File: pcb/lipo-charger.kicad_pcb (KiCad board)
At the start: 2 copper layers, 48 x 48 mm, 37 parts, among them J101 Barrel_Jack, J102 Conn_01x04, J103 Conn_01x03, J104 Conn_01x03, J201 Conn_01x02, J202 Conn_01x02, P101 Polarity, P102 Outline, P103 OSHW, Q201 Q_NMOS_GSD, U101 LM317L_TO92, U201 MP2359, U202 LM358, U203 MAX4377, U204 LM358

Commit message: Massive rework, fully routed
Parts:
- removed C101: 1u, Capacitors_SMD_Round:C_0805
- removed C203: 22u, Capacitors_SMD_Round:C_1206
- removed C204: 0.1u, Capacitors_SMD_Round:C_0603
- removed D202: B230A, Diodes_SMD:D_SMA
- removed D203: B5819, Diodes_SMD:D_SOD-323_HandSoldering
- removed D204: LED, LEDs:LED_0805_HandSoldering
- removed L201: 4.7uH, Inductors_SMD:L_Taiyo-Yuden_NR-50xx
- removed Q201: Q_NMOS_GSD, TO_Combo_Packages:TO_220_247
- removed R102: 330R, Resistors_SMD:R_0603_HandSoldering
- removed R103: 2k, Resistors_SMD:R_0603_HandSoldering
- removed R104, R105: 10k, Resistors_SMD:R_0603_HandSoldering
- removed R202: 100k, Resistors_SMD:R_0603_HandSoldering
- removed R203: 0R025, Sense_Resistors:R_2512_AD_Optimized
- removed R204: 107k, Resistors_SMD:R_0603_HandSoldering
- removed R205: 25.5k, Resistors_SMD:R_0603_HandSoldering
- removed TP101, TP201: TEST, Measurement_Points:Measurement_Point_Round-SMD-Pad_Small
- removed U101: LM317L_TO92, TO_SOT_Packages_THT:TO-92_Inline_Narrow_Oval
- removed U203: MAX4377, Housings_SOIC:SOIC-8_3.9x4.9mm_Pitch1.27mm
- removed U204: LM358, Housings_SOIC:SOIC-8_3.9x4.9mm_Pitch1.27mm
- added C301: 0.1u, Capacitors_SMD_Round:C_0603, F.Cu at (159.5, 109.5)
- added C401: 10u, Capacitors_SMD_Round:C_1206, F.Cu at (138.5, 104.5)
- added C402: 10n, Capacitors_SMD_Round:C_0603, F.Cu at (146.5, 103.0)
- added C403: 22u, Capacitors_SMD_Round:C_1206, F.Cu at (148.5, 101.0)
- added D301: D_Schottky, Diodes_SMD:D_SOD-123, F.Cu at (156.0, 102.0)
- added D401: B230A, Diodes_SMD:D_SMA, F.Cu at (147.5, 111.5)
- added L401: 4.7uH, Inductors_SMD:L_Taiyo-Yuden_NR-50xx, F.Cu at (148.0, 107.0)
- added P104: Fid, Fiducials:Fiducial_1mm_Dia_2.54mm_Outer_CopperTop, F.Cu at (130.0, 120.0)
- added Q301: Q_NMOS_GDS, TO_SOT_Packages_SMD:TO-252-2, F.Cu at (146.5, 84.5)
- added Q302: Q_NMOS_GSD, TO_SOT_Packages_SMD:SOT-23_Handsoldering, F.Cu at (152.0, 92.0)
- added Q501: Q_PMOS_GSD, TO_SOT_Packages_SMD:SOT-23_Handsoldering, F.Cu at (158.5, 83.0)
- added Q502: Q_NMOS_GSD, TO_SOT_Packages_SMD:SOT-23_Handsoldering, F.Cu at (139.5, 98.5)
- added Q503: Q_PMOS_GSD, TO_SOT_Packages_SMD:SOT-23_Handsoldering, F.Cu at (158.5, 88.0)
- added R301: 100R, Resistors_SMD:R_0603_HandSoldering, F.Cu at (166.5, 104.0)
- added R302: 100k, Resistors_SMD:R_0603_HandSoldering, F.Cu at (142.0, 89.0)
- added R303: 100k, Resistors_SMD:R_0603_HandSoldering, F.Cu at (157.5, 98.5)
- added R304: 100k, Resistors_SMD:R_0603_HandSoldering, F.Cu at (154.0, 102.5)
- added R305: 100k, Resistors_SMD:R_0603_HandSoldering, F.Cu at (156.0, 112.5)
- added R401: 107k, Resistors_SMD:R_0603_HandSoldering, F.Cu at (152.0, 102.5)
- added R402: 25.5k, Resistors_SMD:R_0603_HandSoldering, F.Cu at (152.0, 107.5)
- added R501: 100k, Resistors_SMD:R_0603_HandSoldering, F.Cu at (135.5, 98.5)
- added R502: 100k, Resistors_SMD:R_0603_HandSoldering, F.Cu at (162.5, 88.0)
- added U301: LM358, Housings_SOIC:SOIC-8_3.9x4.9mm_Pitch1.27mm, F.Cu at (161.5, 106.0)
- added U401: MP2359, TO_SOT_Packages_SMD:SOT-23-6_Handsoldering, F.Cu at (143.0, 104.5)
- C201: value 10u -> 0.1u; footprint Capacitors_SMD_Round:C_1206 -> Capacitors_SMD_Round:C_0603
- C202: value 10n -> 0.1u
- J101: value Barrel_Jack -> Conn_01x04; footprint Connectors:Barrel_Jack_CUI_PJ-102AH -> Connectors_Molex:Molex_KK-6410-04_04x2.54mm_Straight
- J102: footprint Pin_Headers:Pin_Header_Straight_1x04_Pitch2.54mm -> Connectors_Molex:Molex_KK-6410-04_04x2.54mm_Straight
- J103: value Conn_01x03 -> Conn_01x04; footprint Pin_Headers:Pin_Header_Straight_1x03_Pitch2.54mm -> Connectors_Molex:Molex_KK-6410-04_04x2.54mm_Straight
- J104: footprint Pin_Headers:Pin_Header_Straight_1x03_Pitch2.54mm -> Connectors_Molex:Molex_KK-6410-03_03x2.54mm_Straight
- P101: value Polarity -> Fid; footprint Polarity_Symbols:Polarity_Center_Positive_3mm_SilkScreen -> Fiducials:Fiducial_1mm_Dia_2.54mm_Outer_CopperTop
- R101: value 0R -> 100R
- R201: value 10k -> 0R025; footprint Resistors_SMD:R_0603_HandSoldering -> Sense_Resistors:R_2512_AD_Optimized
- U201: value MP2359 -> LM358; footprint TO_SOT_Packages_SMD:SOT-23-6_Handsoldering -> Housings_SOIC:SOIC-8_3.9x4.9mm_Pitch1.27mm
- U202: value LM358 -> MAX4377
- moved P101 46.8 mm to (163.0, 80.0)
- moved U202 45.3 mm to (164.0, 97.5), turned to 180 degrees
- moved J103 44.5 mm to (172.0, 102.5), turned to 270 degrees
- moved R201 37.9 mm to (160.0, 92.5), turned to 180 degrees
- moved J104 36.6 mm to (172.0, 114.0), turned to 270 degrees
- moved R101 31.9 mm to (149.5, 117.0), turned to 180 degrees
- moved C201 28.0 mm to (162.0, 101.0), turned to 0 degrees
- moved U201 22.0 mm to (161.5, 113.0), turned to 0 degrees
- moved P103 21.9 mm to (139.5, 114.0)
- moved C202 20.5 mm to (159.5, 116.5), turned to 180 degrees
- moved J201 20.0 mm to (170.5, 90.0)
- moved J202 19.9 mm to (171.5, 82.5), turned to 180 degrees
- moved D201 18.8 mm to (154.0, 107.5), turned to 270 degrees
- moved P102 14.8 mm to (127.5, 78.0)
- moved J101 8.20 mm to (131.0, 103.0), turned to 90 degrees
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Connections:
- C201 pad 1: /charger/VIN -> +9VA
- C201 pad 2: GND -> GNDA
- C202 pad 1: Net-(C202-Pad1) -> +9VA
- C202 pad 2: /charger/Vsw -> GNDA
- D201 pad 1: Net-(D201-Pad1) -> /charger/buck/FB
- J101 pad 1: /charger/VIN -> /charger/CHG_EN
- J101 pad 2: GND -> /charger/CHG_AREF
- J101 pad 3: GND -> /charger/MASTER_EN
- J102 pad 1: /charger/CHG_AREF -> +9VA
- J102 pad 2: /charger/LOAD_VREF -> GNDA
- J102 pad 3: /charger/LOAD_AREF -> /charger/VIN
- J102 pad 4: GNDA -> /charger/GNDIN
- J103 pad 1: /charger/CHG_EN -> /charger/LOAD_EN
- J103 pad 2: /charger/LOAD_EN -> /charger/LOAD_VREF
- J103 pad 3: GNDA -> /charger/LOAD_AREF
- J201 pad 2: GND -> /charger/GNDIN
- J202 pad 2: GND -> /charger/GNDIN
- R101 pad 1: GND -> /charger/GNDIN
- R201 pad 1: Net-(R201-Pad1) -> /charger/BATPLUS
- R201 pad 2: Net-(D203-Pad2) -> Net-(R201-Pad2)
- U201 pad 1: Net-(C202-Pad1) -> Net-(D201-Pad2)
- U201 pad 2: GND -> /charger/OUT1
- U201 pad 3: Net-(D201-Pad1) -> /charger/CHG_AREF
- U201 pad 4: /charger/CHG_EN -> GNDA
- U201 pad 5: /charger/VIN -> GNDA
- U201 pad 6: /charger/Vsw -> GNDA
- U202 pad 1: Net-(D204-Pad1) -> /charger/OUT1
- U202 pad 2: Net-(D201-Pad1) -> Net-(R201-Pad2)
- U202 pad 3: /charger/LOAD_VREF -> Net-(R201-Pad3)
- U202 pad 5: /charger/LOAD_AREF -> Net-(R201-Pad2)
- U202 pad 6: /charger/OUT2 -> Net-(R201-Pad3)
- U202 pad 7: Net-(R201-Pad1) -> /charger/OUT2
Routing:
- net /charger/GNDIN: track 0.00 -> 74.9 mm, vias 0 -> 27
- net GNDA: track 123.0 -> 69.0 mm, vias 7 -> 5
- net Net-(D201-Pad1): track 46.2 -> 0.00 mm, vias 2 -> 0
- net Net-(D301-Pad2): track 0.00 -> 36.0 mm, vias 0 -> 2
- net +9VA: track 97.7 -> 62.3 mm, vias 1 -> 2
- net GND: track 34.9 -> 0.00 mm, vias 21 -> 0
- net Net-(Q501-Pad1): track 0.00 -> 32.1 mm, vias 0 -> 2
- net /charger/VIN: track 44.0 -> 14.4 mm, vias 18 -> 0
- net /charger/OUT2: track 55.0 -> 26.1 mm, vias 2 -> 4
- net /charger/CHG_AREF: track 31.1 -> 58.8 mm, vias 0 -> 2
- net /charger/Ind_out: track 26.5 -> 0.00 mm, vias 10 -> 0
- net /charger/output_disconnect/LOAD_CHARGE: track 0.00 -> 24.2 mm
- net Net-(R203-Pad2): track 22.4 -> 0.00 mm, vias 3 -> 0
- net Net-(D203-Pad2): track 21.7 -> 0.00 mm
- net /charger/buck/FB: track 0.00 -> 18.2 mm, vias 0 -> 2
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- added copper zone on B.Cu, net /charger/BATPLUS
- added copper zone on B.Cu, net /charger/GNDIN
- added copper zone on F.Cu, net /charger/GNDIN
- added copper zone on F.Cu, net /charger/buck/Vsw
- added copper zone on F.Cu, net /charger/output_disconnect/BATT
- added copper zone on F.Cu, net /charger/output_disconnect/LOAD_CHARGE
- added copper zone on B.Cu, net GNDA
- added copper zone on F.Cu, net Net-(Q301-Pad3)
- added copper zone on F.Cu, net Net-(Q501-Pad2)
- removed copper zone on B.Cu, net /charger/Ind_out
- removed copper zone on F.Cu, net /charger/Ind_out
- removed copper zone on B.Cu, net /charger/VIN
- removed copper zone on F.Cu, net /charger/Vsw
- removed copper zone on B.Cu, net GND
- removed copper zone on F.Cu, net GND
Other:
- board text added: "CC-BY"
- board text added: "GNDA MASTER_EN CHG_AREF CHG_EN"
- board text added: "LOAD_EN LOAD_VREF LOAD_AREF GNDA"
- board text added: "OUT1 OUT2 GNDA"
- board text added: "Power GND Power VIN GNDA +9VA"
- board text added: "github.com/thatch/lipo-charger"
- board text removed: "%%gitversion%%"
- board text removed: "-"
- board text removed: "Tim Hatch"
- board text removed: "github.com/thatch/ lipo-charger"

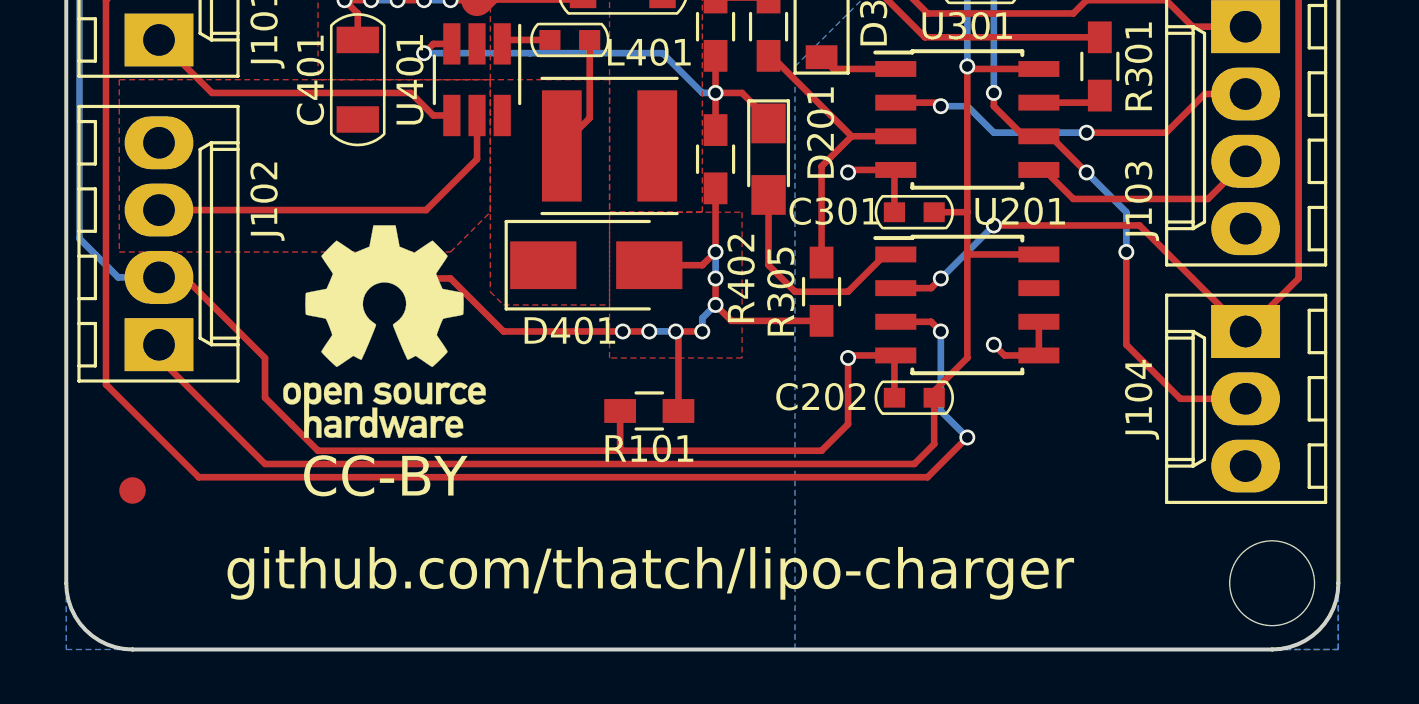
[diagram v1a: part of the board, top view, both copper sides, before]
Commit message: Add gitversion to pcb, minor tweaks
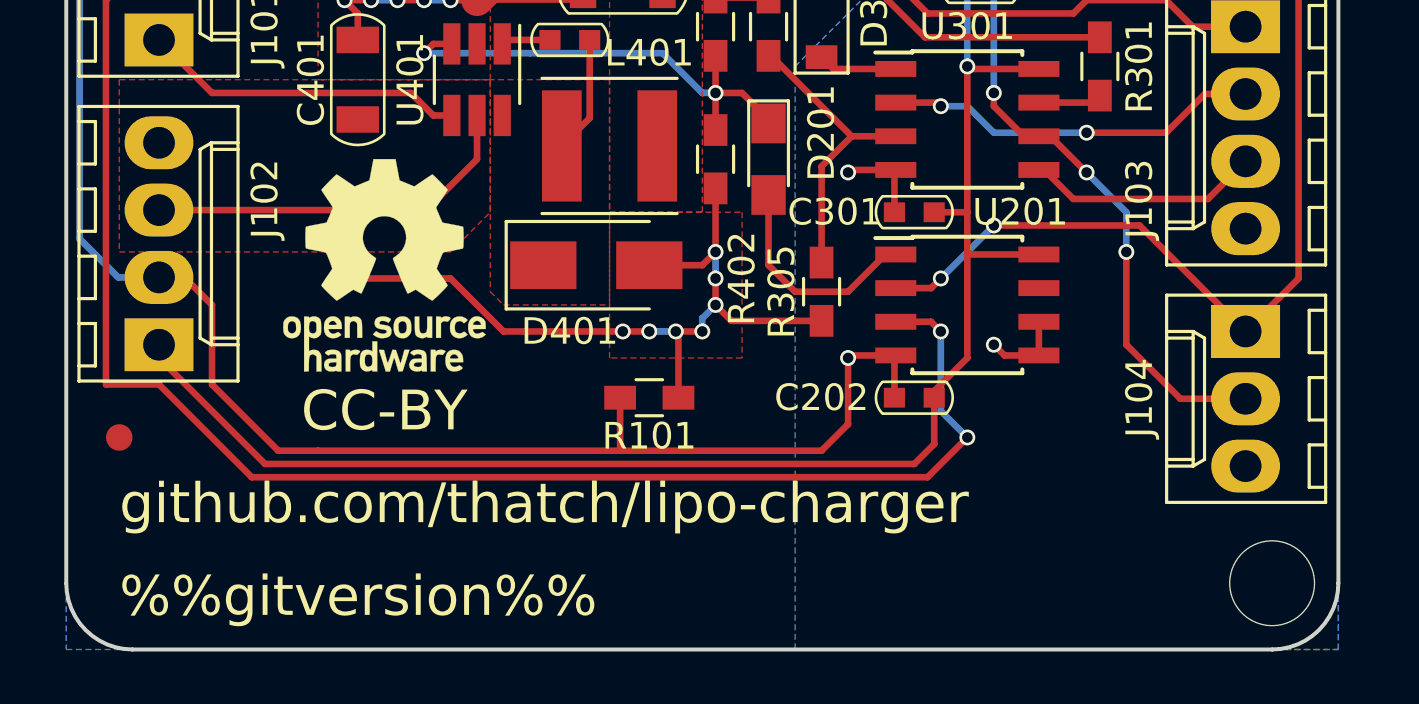
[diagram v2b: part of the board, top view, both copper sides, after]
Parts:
- moved P103 2.50 mm to (139.5, 111.5)
- moved P104 2.06 mm to (129.5, 118.0)
- moved R101 0.50 mm to (149.5, 116.5)
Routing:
- net GNDA: track 69.0 -> 70.3 mm
- net /charger/GNDIN: track 74.9 -> 74.4 mm
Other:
- board text added: "%%gitversion%%"
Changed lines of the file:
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@@
     (area 0 0 0 0)
     (thickness 1.6)
-    (drawings 9)
-    (tracks 334)
+    (drawings 10)
+    (tracks 335)
     (zones 0)
     (modules 40)
@@
   )
   (module Symbols:OSHW-Logo_7.5x8mm_SilkScreen (layer F.Cu)
-    (at 139.5 114)
+    (at 139.5 111.5)
     (descr "Open Source Hardware Logo")
     (tags "Logo OSHW")
@@
   )
   (module Resistors_SMD:R_0603_HandSoldering (layer F.Cu)
-    (at 149.5 117 180)
+    (at 149.5 116.5 180)
     (descr "Resistor SMD 0603, hand soldering")
     (tags "resistor 0603")
@@
   )
   (module Fiducials:Fiducial_1mm_Dia_2.54mm_Outer_CopperTop (layer F.Cu)
-    (at 130 120)
+    (at 129.5 118)
     (descr "Circular Fiducial, 1mm bare copper top; 2.54mm keepout")
     (tags marker)
@@
       (solder_mask_margin 0.77) (clearance 0.77))
   )
-  (gr_text CC-BY (at 139.5 119.5) (layer F.SilkS)
+  (gr_text %%gitversion%% (at 129.5 124) (layer F.SilkS)
+    (effects (font (size 1.5 1.5) (thickness 0.3)) (justify left))
+  )
+  (gr_text CC-BY (at 139.5 117) (layer F.SilkS)
     (effects (font (size 1.5 1.5) (thickness 0.3)))
   )
@@
     (effects (font (size 1.5 1.5) (thickness 0.3)) (justify left mirror))
   )
-  (gr_text github.com/thatch/lipo-charger (at 149.5 123) (layer F.SilkS)
-    (effects (font (size 1.5 1.5) (thickness 0.3)))
+  (gr_text github.com/thatch/lipo-charger (at 129.5 120.5) (layer F.SilkS)
+    (effects (font (size 1.5 1.5) (thickness 0.3)) (justify left))
   )
   (gr_circle (center 130 80.5) (end 133 80.5) (layer F.Fab) (width 0.2))
@@
   (segment (start 151.5 95.5) (end 151.05 95.05) (width 0.25) (layer F.Cu) (net 4))
   (segment (start 151.05 95.05) (end 151.05 93.5) (width 0.25) (layer F.Cu) (net 4))
+  (segment (start 129 116) (end 131 116) (width 0.25) (layer F.Cu) (net 5))
+  (segment (start 131 116) (end 134.5 119.5) (width 0.25) (layer F.Cu) (net 5))
   (segment (start 131 100.46) (end 130.04 100.46) (width 0.25) (layer F.Cu) (net 5))
   (segment (start 130.04 100.46) (end 129 101.5) (width 0.25) (layer F.Cu) (net 5))
@@
   (via (at 161.5 118) (size 0.6) (drill 0.4) (layers F.Cu B.Cu) (net 5))
   (segment (start 160 119.5) (end 161.5 118) (width 0.25) (layer F.Cu) (net 5))
-  (segment (start 132.5 119.5) (end 160 119.5) (width 0.25) (layer F.Cu) (net 5))
-  (segment (start 129 116) (end 132.5 119.5) (width 0.25) (layer F.Cu) (net 5))
+  (segment (start 134.5 119.5) (end 160 119.5) (width 0.25) (layer F.Cu) (net 5))
   (segment (start 129 101.5) (end 129 116) (width 0.25) (layer F.Cu) (net 5))
   (segment (start 131 100.46) (end 129.96 100.46) (width 0.25) (layer F.Cu) (net 5))
@@
   (segment (start 165.5 109) (end 170.58 109) (width 0.25) (layer F.Cu) (net 7))
   (segment (start 171.675 107.905) (end 172 107.58) (width 0.25) (layer F.Cu) (net 7))
-  (segment (start 148.4 117) (end 148.4 118.5) (width 0.25) (layer F.Cu) (net 8))
+  (segment (start 133 113) (end 133 116) (width 0.25) (layer F.Cu) (net 8))
+  (segment (start 135.5 118.5) (end 137 118.5) (width 0.25) (layer F.Cu) (net 8))
+  (segment (start 133 116) (end 135.5 118.5) (width 0.25) (layer F.Cu) (net 8))
+  (segment (start 148.4 116.5) (end 148.4 118.5) (width 0.25) (layer F.Cu) (net 8) (status 10))
   (segment (start 148.4 118.5) (end 148.5 118.5) (width 0.25) (layer F.Cu) (net 8))
   (segment (start 131 111.96) (end 131.96 111.96) (width 0.25) (layer F.Cu) (net 8))
-  (segment (start 131.96 111.96) (end 135 115) (width 0.25) (layer F.Cu) (net 8))
-  (segment (start 135 116.5) (end 136 117.5) (width 0.25) (layer F.Cu) (net 8))
-  (segment (start 135 115) (end 135 116.5) (width 0.25) (layer F.Cu) (net 8))
+  (segment (start 131.96 111.96) (end 133 113) (width 0.25) (layer F.Cu) (net 8))
   (segment (start 131 95.38) (end 129.62 95.38) (width 0.25) (layer B.Cu) (net 8))
   (segment (start 129.46 111.96) (end 131 111.96) (width 0.25) (layer B.Cu) (net 8))
@@
   (segment (start 137 118.5) (end 148.5 118.5) (width 0.25) (layer F.Cu) (net 8))
   (segment (start 148.5 118.5) (end 156 118.5) (width 0.25) (layer F.Cu) (net 8))
-  (segment (start 136 117.5) (end 137 118.5) (width 0.25) (layer F.Cu) (net 8))
   (segment (start 164.2 114.905) (end 162.905 114.905) (width 0.25) (layer F.Cu) (net 8))
   (via (at 162.5 114.5) (size 0.6) (drill 0.4) (layers F.Cu B.Cu) (net 8))
@@
   (via (at 170 92.5) (size 0.6) (drill 0.4) (layers F.Cu B.Cu) (net 12))
   (segment (start 170.3 92.2) (end 170 92.5) (width 0.25) (layer B.Cu) (net 12))
-  (segment (start 150.6 117) (end 150.6 114.1) (width 0.25) (layer F.Cu) (net 13))
+  (segment (start 150.6 116.5) (end 150.6 114.1) (width 0.25) (layer F.Cu) (net 13) (status 10))
   (segment (start 150.6 114.1) (end 150.5 114) (width 0.25) (layer F.Cu) (net 13))
   (segment (start 167.54 82.5) (end 165.5 82.5) (width 0.4) (layer F.Cu) (net 13))

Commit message: Fixup url and add license
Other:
- board text added: "github.com/google/makerspace-lipo-charger"
- board text removed: "github.com/thatch/lipo-charger"
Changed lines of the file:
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@@
-(kicad_pcb (version 4) (host pcbnew 4.0.7)
+(kicad_pcb (version 4) (host pcbnew 4.0.6+dfsg1-1)
   (general
     (links 87)
     (no_connects 0)
-    (area 0 0 0 0)
+    (area 126.899999 65.325 177.125001 126.600001)
     (thickness 1.6)
     (drawings 10)
@@
   )
   (setup
-    (last_trace_width 0.4)
+    (last_trace_width 0.25)
     (user_trace_width 0.4)
     (user_trace_width 1.2)
@@
   )
   (gr_text %%gitversion%% (at 129.5 124) (layer F.SilkS)
-    (effects (font (size 1.5 1.5) (thickness 0.3)) (justify left))
+    (effects (font (size 1.2 1.1) (thickness 0.275)) (justify left))
   )
   (gr_text CC-BY (at 139.5 117) (layer F.SilkS)
@@
     (effects (font (size 1.5 1.5) (thickness 0.3)) (justify left mirror))
   )
-  (gr_text github.com/thatch/lipo-charger (at 129.5 120.5) (layer F.SilkS)
-    (effects (font (size 1.5 1.5) (thickness 0.3)) (justify left))
+  (gr_text github.com/google/makerspace-lipo-charger (at 129.5 120.5) (layer F.SilkS)
+    (effects (font (size 1.2 1.1) (thickness 0.275)) (justify left))
   )
   (gr_circle (center 130 80.5) (end 133 80.5) (layer F.Fab) (width 0.2))
